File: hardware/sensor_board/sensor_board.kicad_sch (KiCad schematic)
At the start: 26 parts, among them J1 CORTEX-SWD-6, J2 Conn_01x04_MountingPin, Q1 SI2337DS-T1-BE3, Q2 SI2337DS-T1-BE3, U1 ATSAMC21E17A, U2 TCAN332G, Y1 Resonator

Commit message: updated pcb
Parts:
- added D2: MMBZ15VALT1G, Package_TO_SOT_SMD:SOT-23, symbol Device:D_Zener_Dual_CommonAnode_KKA_Parallel
- added Q3: BSH203,215, Package_TO_SOT_SMD:SOT-23, symbol Device:Q_PMOS_GSD
- added R9: 100k, Resistor_SMD:R_0402_1005Metric, symbol Device:R
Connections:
- net +36V: now also D2.1 (K), Q3.2 (S); no longer J2.2 (Pin_2)
- net 5VSW_SIG: now also U1.1 (PA00); no longer U1.3 (PA02)
- net GND: now also R9.2
- net GPIO.0: now also U1.3 (PA02); no longer U1.1 (PA00)
- net GPIO.1: now also U1.4 (PA03); no longer U1.2 (PA01)
- net VDDSW_SIG: now also U1.2 (PA01); no longer U1.4 (PA03)
- new net: D2.3 (A), Q3.1 (G), R9.1
- new net: J2.2 (Pin_2), Q3.3 (D)
- no-connect marks 11 -> 12
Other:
- moved on the sheet: J2

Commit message: finished board
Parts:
- removed D1: RCLAMP0502BA, Package_TO_SOT_SMD:SOT-416, symbol Power_Protection:RCLAMP0502BA
- added D1: PESD2CAN, Package_TO_SOT_SMD:SOT-23, symbol Power_Protection:NUP2105L
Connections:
- net CAN+: now also J2.3 (Pin_3), D1.1 (K); no longer J2.4 (Pin_4)
- net CAN-: now also J2.2 (Pin_2), D1.2 (K); no longer J2.3 (Pin_3)
- net GND: now also D1.3 (A)
- net at Q3.3 (D): now also J2.4 (Pin_4); no longer J2.2 (Pin_2)
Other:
- note removed: "CAP 10uf 100nf"
- moved on the sheet: J2

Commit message: researched parts
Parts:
- C1: MOUSER_NO (none) -> 81-GRM155R71H103KA8D
- C2, C7, C9: MOUSER_NO (none) -> 81-GRM188R60J106ME4D
- C3, C4, C6, C8: MOUSER_NO (none) -> 81-GCJ188R71H104KA2D
- C5: MOUSER_NO (none) -> 81-LLR185C70G105ME3L
- D2: MOUSER_NO (none) -> 863-SZMMBZ15VALT1G
- J1, R1, R2, R3, R4, R5, R6, R7, R8, R9, U1, U2, Y1: MOUSER_NO (none) -> DO NOT ORDER
- J2: footprint Connector_Molex:Molex_PicoBlade_53261-0471_1x04-1MP_P1.25mm_Horizontal -> Connector_Molex:Molex_PicoBlade_53047-0410_1x04_P1.25mm_Vertical; Farnell_NO (none) -> 9733060
- Q1, Q2: MOUSER_NO (none) -> 78-SI2337DS-T1-BE3
- Q3: MOUSER_NO (none) -> 771-BSH203215
- TP1: MOUSER_NO (none) -> 534-5015

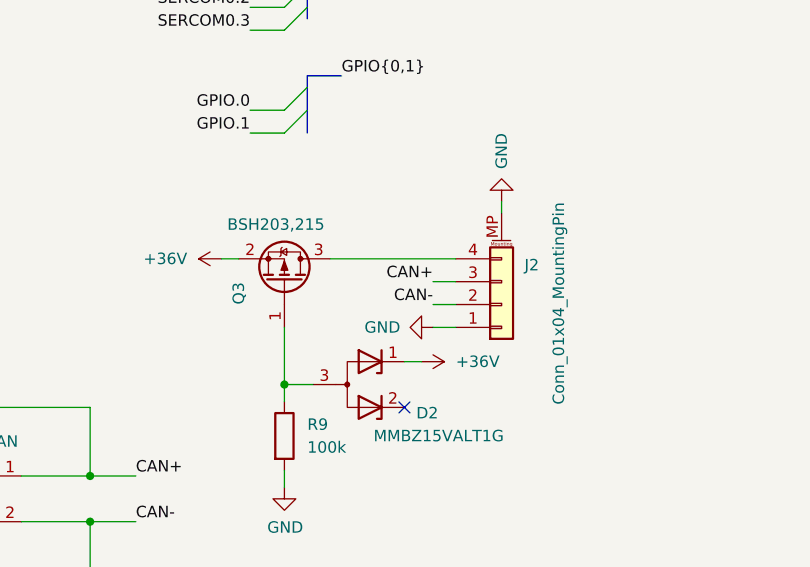
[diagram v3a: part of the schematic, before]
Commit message: updated board with new connector
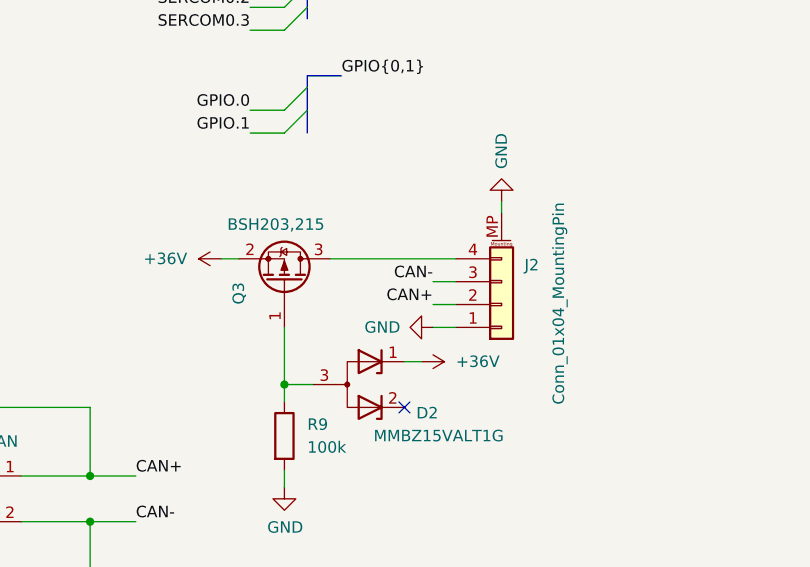
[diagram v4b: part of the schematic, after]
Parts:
- J2: footprint Connector_Molex:Molex_PicoBlade_53047-0410_1x04_P1.25mm_Vertical -> Connector_Molex:Molex_CLIK-Mate_502382-0470_1x04-1MP_P1.25mm_Vertical
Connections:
- net CAN+: now also J2.2 (Pin_2); no longer J2.3 (Pin_3)
- net CAN-: now also J2.3 (Pin_3); no longer J2.2 (Pin_2)

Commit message: changed to tag connect due to chip shortage
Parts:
- J1: footprint Connector_Hirose:Hirose_DF11-6DP-2DSA_2x03_P2.00mm_Vertical -> Connector:Tag-Connect_TC2030-IDC-NL_2x03_P1.27mm_Vertical

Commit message: some stuff!
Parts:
- J1: symbol ownLib:CORTEX-SWD-6 -> ownLib:CORTEX-SWD-6-TAG
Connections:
- net CAN_{RX}: now also U1.24 (PA25); no longer U1.23 (PA24)
- net CAN_{TX}: now also U1.23 (PA24); no longer U1.22 (PA23)
- net GND: now also J1.5 (GND); no longer J1.2 (GND)
- net SWCLK: now also J1.4 (SWCLK); no longer J1.3 (SWCLK)
- net SWDIO: now also J1.2 (SWDIO); no longer J1.5 (SWDIO)
- net VDD: now also J1.1 (VCC); no longer J1.6 (VCC)
- net ~{RESET}: now also J1.3 (~{RESET}); no longer J1.4 (~{RESET})
